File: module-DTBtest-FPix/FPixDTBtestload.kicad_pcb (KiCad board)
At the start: 4 copper layers, 100 x 40 mm, 23 parts, among them J1 CONN-SMK20, P10 VD, P14 GND, P4 VA

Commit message: Improved grounding
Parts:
- R1, R2: value R_0603_HandSoldering -> 10k 0.1%
- R3: value R_Caddock_USF371 -> 25 MEG
- R4, R5: value R_2512_HandSoldering -> 3.2
- R6, R7: value R_2512_HandSoldering -> 4.8
- turned R4 to 270 degrees
- turned R5 to 270 degrees
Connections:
- J1 pad 1: (no net) -> RTD-
- J1 pad 11: (no net) -> TBM_Clk_In+
- J1 pad 13: (no net) -> TBM_Trig_In-
- J1 pad 15: (no net) -> TBM_Trig_In+
- J1 pad 19: HV -> Net-(J1-Pad19)
- J1 pad 25: (no net) -> TBM_SD_In-
- J1 pad 27: (no net) -> TBM_SD_In+
- J1 pad 29: (no net) -> TBM_RDa_Out-
- J1 pad 3: (no net) -> RTD+
- J1 pad 31: (no net) -> TBM_RDa_Out+
- J1 pad 37: (no net) -> TBM_Out_A-
- J1 pad 39: (no net) -> TBM_Out_A+
- J1 pad 9: (no net) -> TBM_Clk_In-
- JP1 pad 1: GND -> RTD-
- JP1 pad 2: GND -> Net-(JP1-Pad2)
- R1 pad 1: (no net) -> RTD+
- R1 pad 2: (no net) -> Net-(JP1-Pad2)
- R2 pad 1: (no net) -> Net-(JP1-Pad2)
- R2 pad 2: (no net) -> RTD-
- R3 pad 1: (no net) -> Net-(J1-Pad19)
- R3 pad 2: (no net) -> GND
- R4 pad 1: (no net) -> GND
- R4 pad 2: (no net) -> VA
- R5 pad 1: (no net) -> GND
- R5 pad 2: (no net) -> VA
- R6 pad 1: (no net) -> VD
- R6 pad 2: (no net) -> GND
- R7 pad 1: (no net) -> VD
- R7 pad 2: (no net) -> GND
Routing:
- net (no net): track 70.7 -> 0.00 mm
- net VD: track 221.3 -> 151.0 mm
- net RTD+: track 0.00 -> 70.3 mm
- net Net-(JP1-Pad2): track 0.00 -> 70.0 mm
- net RTD-: track 0.00 -> 16.2 mm
- net Net-(J1-Pad19): track 0.00 -> 14.2 mm
- net HV: track 25.2 -> 11.0 mm
- net N-0000016: track 19.7 -> 9.19 mm
- net GND: track 102.5 -> 101.8 mm, vias 0 -> 19
- added copper zone on B.Cu, net GND
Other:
- copper layers 4 -> 2

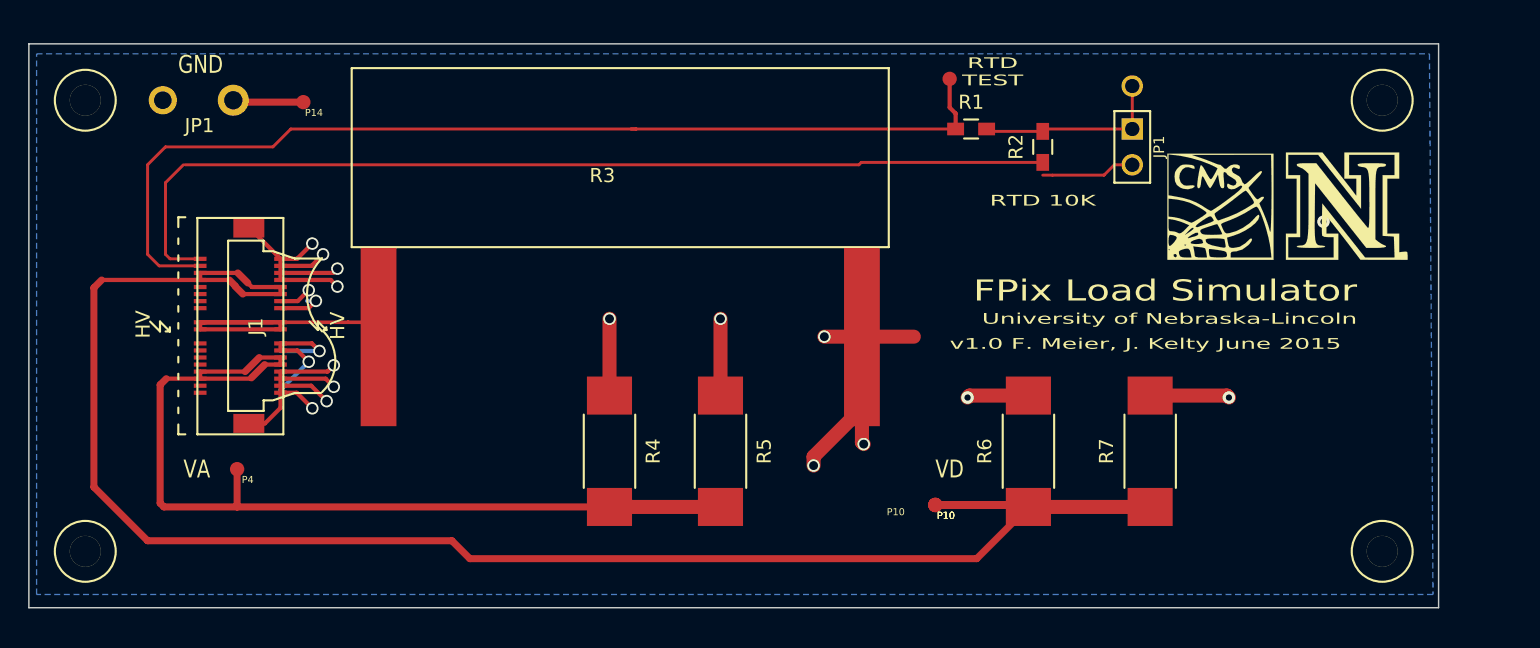
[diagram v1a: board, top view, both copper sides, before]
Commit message: Layout ok. TODO: rotate connector and re-layout everything...
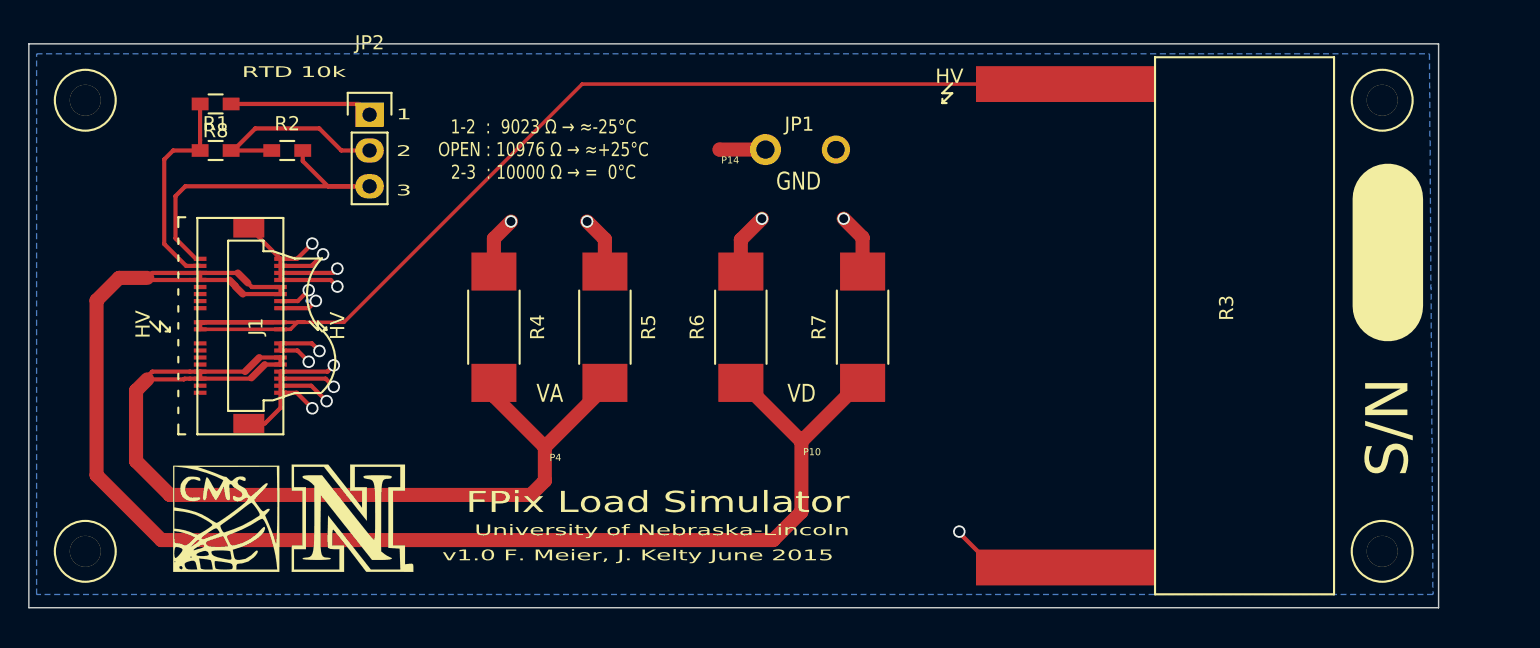
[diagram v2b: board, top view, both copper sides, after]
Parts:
- removed the JP1 at (128.3, 67.3)
- removed the P10 at (110.7, 92.5)
- removed the P10 at (114.3, 92.7) (x2)
- added R8: 41.2k 0.1%, Resistors_SMD:R_0603_HandSoldering, F.Cu at (63.2, 64.3)
- JP2: value JUMPER -> JUMPER3; footprint PIN_ARRAY_2X1 -> Pin_Headers:Pin_Header_Straight_1x03; moved to F.Cu
- R2: value 10k 0.1% -> 976 0.1%
- moved G*** 73.9 mm to (64.0, 93.7)
- moved G*** 73.9 mm to (73.0, 93.7)
- moved JP2 54.3 mm to (74.2, 65.0), turned to 0 degrees
- moved R1 53.6 mm to (63.2, 67.6)
- moved R2 53.6 mm to (68.3, 67.6), turned to 0 degrees
- moved R3 45.1 mm to (135.6, 80.0), turned to 270 degrees
- moved JP1 42.9 mm to (104.8, 67.5), turned to 180 degrees
- moved P14 29.7 mm to (99.0, 67.5)
- moved R6 22.2 mm to (100.5, 80.1)
- moved R7 22.2 mm to (109.1, 80.1)
- moved P4 21.9 mm to (86.6, 88.6)
- moved R4 12.0 mm to (83.0, 80.1)
- moved R5 12.0 mm to (90.9, 80.1)
- moved P10 10.5 mm to (104.8, 88.2)
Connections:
- J1 pad 19: Net-(J1-Pad19) -> HV
- JP1 pad 1: RTD- -> GND
- JP1 pad 2: Net-(JP1-Pad2) -> GND
- JP2 pad 2: N-0000016 -> Net-(JP2-Pad2)
- R1 pad 2: Net-(JP1-Pad2) -> Net-(JP2-Pad2)
- R2 pad 1: Net-(JP1-Pad2) -> Net-(JP2-Pad2)
- R3 pad 1: Net-(J1-Pad19) -> HV
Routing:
- net HV: track 11.0 -> 82.0 mm
- net Net-(JP1-Pad2): track 70.0 -> 0.00 mm
- net RTD+: track 70.3 -> 15.3 mm
- net VD: track 151.0 -> 107.4 mm
- net GND: track 101.8 -> 79.4 mm, vias 19 -> 17
- net Net-(J1-Pad19): track 14.2 -> 0.00 mm
- net Net-(JP2-Pad2): track 0.00 -> 14.0 mm
- net Net-(JP2-Pad1): track 0.00 -> 10.1 mm
- net RTD-: track 16.2 -> 25.6 mm
- net N-0000016: track 9.19 -> 0.00 mm
- net VA: track 75.4 -> 72.4 mm
- net (no net): vias 1 -> 0
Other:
- net class 115Ohm removed
- net class 60Ohm removed
- net class RTDnet added: clearance 0.1, trace_width 0.3, via_dia 0.889, via_drill 0.635
- net class power: clearance 0.198 -> 0.1
- board text added: "1"
- board text added: "1-2 : 9023 Ω → ≈-25°C OPEN : 10976 Ω → ≈+25°C 2-3 : 10000 Ω → = 0°C"
- board text added: "2"
- board text added: "3"
- board text added: "RTD 10k"
- board text added: "S/N"
- board text removed: "RTD 10K"
- board text removed: "RTD TEST"

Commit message: first draft of connector on the right unfinished
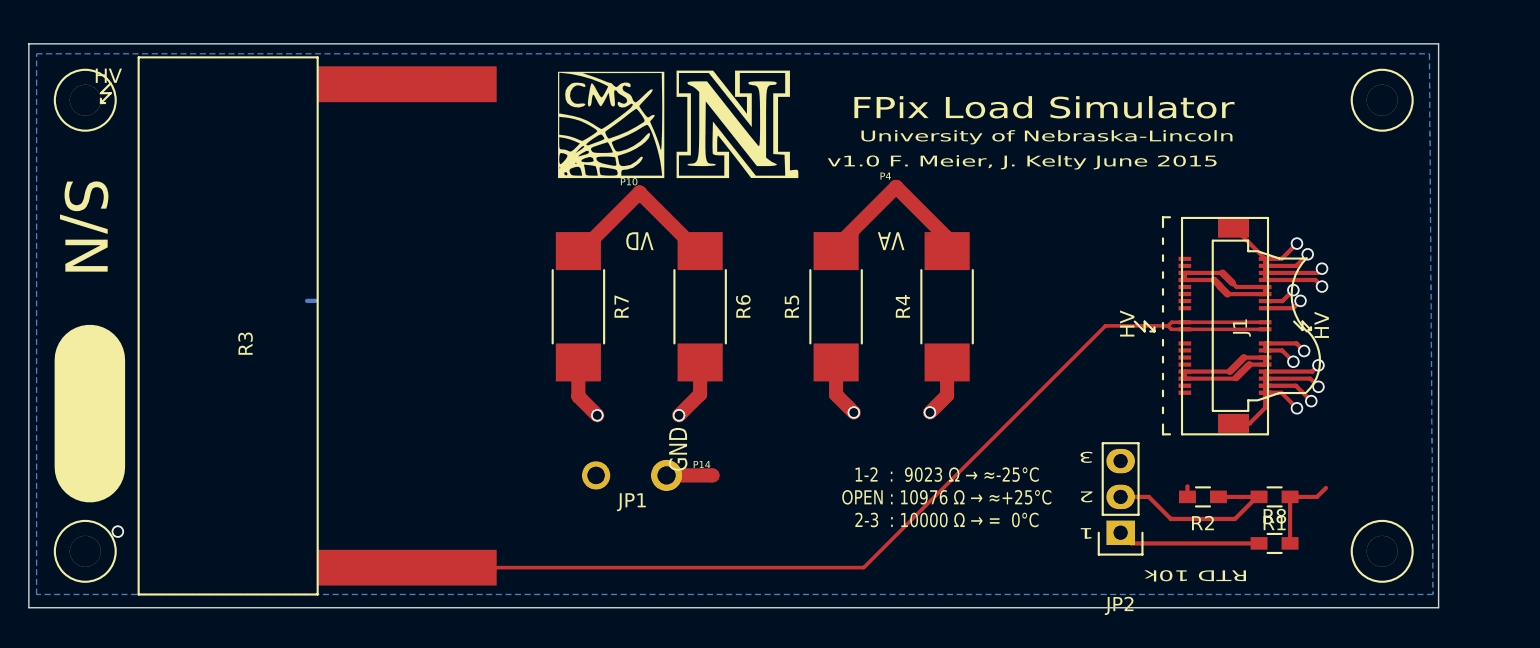
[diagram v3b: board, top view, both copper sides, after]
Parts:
- moved R8 81.3 mm to (138.4, 95.4), turned to 0 degrees
- moved R1 79.0 mm to (138.4, 92.1), turned to 180 degrees
- moved R3 70.8 mm to (64.8, 80.0), turned to 90 degrees
- moved J1 69.8 mm to (134.8, 80.0)
- moved R2 69.5 mm to (133.3, 92.1), turned to 180 degrees
- moved JP2 61.0 mm to (127.4, 94.7), turned to 180 degrees
- moved G*** 39.1 mm to (91.3, 65.7)
- moved G*** 39.1 mm to (100.3, 65.7)
- moved R4 32.2 mm to (115.1, 78.7), turned to 90 degrees
- moved P4 31.0 mm to (111.5, 70.2), turned to 180 degrees
- moved JP1 26.1 mm to (92.7, 90.6), turned to 0 degrees
- moved P14 23.1 mm to (98.5, 90.6), turned to 180 degrees
- moved P10 21.1 mm to (93.3, 70.5), turned to 180 degrees
- moved R7 20.2 mm to (89.0, 78.7), turned to 270 degrees
- moved R5 16.5 mm to (107.3, 78.7), turned to 90 degrees
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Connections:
- J1 pad 1: RTD- -> (no net)
- J1 pad 10: VD -> VA
- J1 pad 11: TBM_Clk_In+ -> (no net)
- J1 pad 12: VD -> VA
- J1 pad 13: TBM_Trig_In- -> (no net)
- J1 pad 15: TBM_Trig_In+ -> (no net)
- J1 pad 25: TBM_SD_In- -> (no net)
- J1 pad 27: TBM_SD_In+ -> (no net)
- J1 pad 29: TBM_RDa_Out- -> (no net)
- J1 pad 3: RTD+ -> (no net)
- J1 pad 30: VA -> VD
- J1 pad 31: TBM_RDa_Out+ -> (no net)
- J1 pad 32: VA -> VD
- J1 pad 33: VA -> VD
- J1 pad 35: VA -> VD
- J1 pad 37: TBM_Out_A- -> RTD-
- J1 pad 39: TBM_Out_A+ -> RTD+
- J1 pad 5: VD -> VA
- J1 pad 7: VD -> VA
- J1 pad 9: TBM_Clk_In- -> (no net)
- JP2 pad 1: Net-(JP2-Pad1) -> (no net)
- JP2 pad 2: Net-(JP2-Pad2) -> (no net)
- R1 pad 2: Net-(JP2-Pad2) -> (no net)
- R2 pad 1: Net-(JP2-Pad2) -> (no net)
- R2 pad 2: RTD- -> (no net)
- R8 pad 1: Net-(JP2-Pad1) -> (no net)
- R8 pad 2: RTD+ -> (no net)
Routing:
- net VD: track 107.4 -> 25.3 mm
- net VA: track 72.4 -> 25.6 mm
- net (no net): track 0.00 -> 25.8 mm, vias 0 -> 1
- net RTD-: track 25.6 -> 0.00 mm
- net Net-(JP2-Pad2): track 14.0 -> 0.00 mm
- net Net-(JP2-Pad1): track 10.1 -> 0.00 mm
- net GND: track 79.4 -> 70.1 mm, vias 17 -> 16
- net RTD+: track 15.3 -> 6.11 mm
- net HV: track 82.0 -> 75.1 mm

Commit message: first draft of potentially finished load board? please check
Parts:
- removed JP2: JUMPER3, Pin_Headers:Pin_Header_Straight_1x03
- removed P10: VD, testpad
- removed P4: VA, testpad
- added RTD Select: JUMPER3, Pin_Headers:Pin_Header_Straight_1x03, F.Cu at (127.6, 94.7)
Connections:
- R1 pad 2: (no net) -> Net-(JP2-Pad2)
- R2 pad 1: (no net) -> Net-(JP2-Pad2)
- R2 pad 2: (no net) -> RTD-
- R8 pad 1: (no net) -> Net-(JP2-Pad1)
- R8 pad 2: (no net) -> RTD+
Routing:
- net VD: track 25.3 -> 102.7 mm
- net (no net): track 25.8 -> 0.00 mm, vias 1 -> 0
- net RTD-: track 0.00 -> 19.7 mm
- net VA: track 25.6 -> 42.8 mm
- net GND: track 70.1 -> 86.4 mm, vias 16 -> 17
- net RTD+: track 6.11 -> 20.9 mm
- net Net-(JP2-Pad2): track 0.00 -> 11.7 mm
- net Net-(JP2-Pad1): track 0.00 -> 10.00 mm
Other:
- board text added: "2-3 : 10000 Ω → = 0°C OPEN : 10976 Ω → ≈+25°C 1-2 : 9023 Ω → ≈-25°C"
- board text added: "v1.0 F. Meier, J. Kelty July 2015"
- board text removed: "1-2 : 9023 Ω → ≈-25°C OPEN : 10976 Ω → ≈+25°C 2-3 : 10000 Ω → = 0°C"
- board text removed: "RTD 10k"
- board text removed: "v1.0 F. Meier, J. Kelty June 2015"
